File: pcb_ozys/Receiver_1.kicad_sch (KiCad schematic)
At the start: 16 parts, among them Q4 2N7002, Q6 AO3401A, U1 INA826AIDR

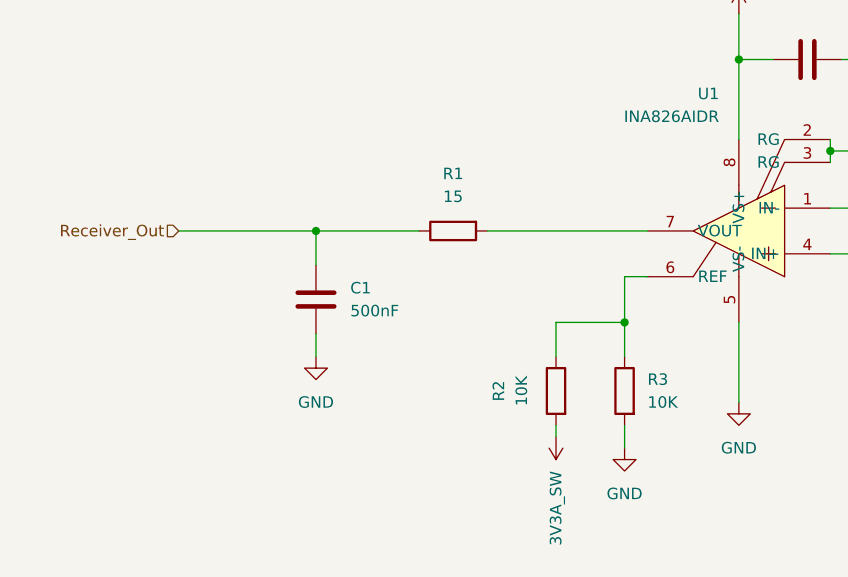
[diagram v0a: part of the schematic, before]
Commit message: Started PCBs fixed connectors
- Fixed Bypass on CAN
- Seperated SG connectors from 2x1 to 1x1
- Rough Draft of Epsilon
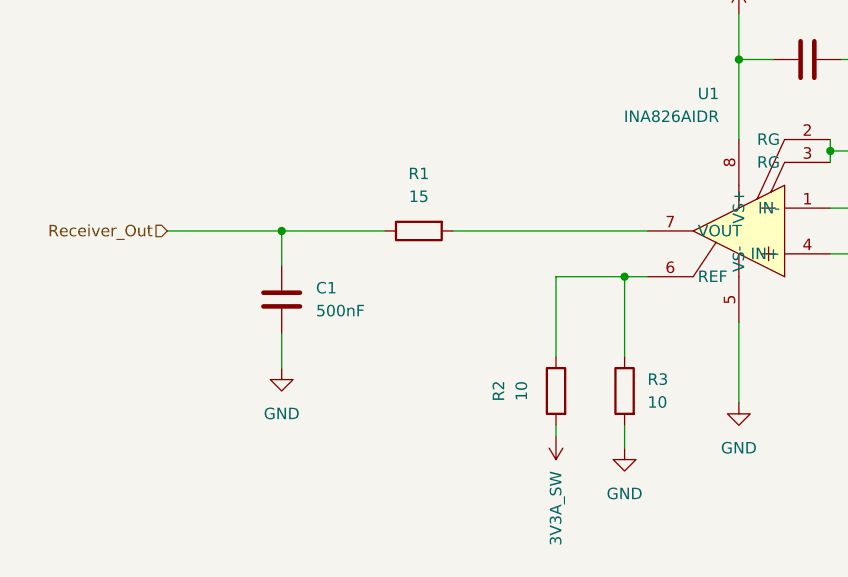
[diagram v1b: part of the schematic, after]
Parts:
- R2, R3: value 10K -> 10
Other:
- moved on the sheet: C1, R1
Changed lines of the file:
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@@
 	(paper "A4")
+	(junction
+		(at 129.54 130.81)
+		(diameter 0)
+		(color 0 0 0 0)
+	)
 	(junction
 		(at 100.33 71.12)
@@
 	)
 	(junction
-		(at 129.54 135.89)
-		(diameter 0)
-		(color 0 0 0 0)
-	)
-	(junction
 		(at 171.45 128.27)
 		(diameter 0)
@@
 	)
 	(junction
-		(at 95.25 125.73)
+		(at 91.44 125.73)
 		(diameter 0)
 		(color 0 0 0 0)
@@
 	(wire
 		(pts
-			(xy 80.01 125.73) (xy 95.25 125.73)
+			(xy 78.74 125.73) (xy 91.44 125.73)
 		)
 		(stroke
@@
 	(wire
 		(pts
-			(xy 95.25 125.73) (xy 106.68 125.73)
+			(xy 91.44 125.73) (xy 102.87 125.73)
 		)
 		(stroke
@@
 	(wire
 		(pts
-			(xy 95.25 129.54) (xy 95.25 125.73)
+			(xy 91.44 129.54) (xy 91.44 125.73)
 		)
 		(stroke
@@
 	(wire
 		(pts
-			(xy 121.92 135.89) (xy 121.92 139.7)
+			(xy 121.92 130.81) (xy 121.92 139.7)
 		)
 		(stroke
@@
 	(wire
 		(pts
-			(xy 129.54 135.89) (xy 129.54 130.81)
+			(xy 129.54 130.81) (xy 129.54 139.7)
 		)
 		(stroke
@@
 	(wire
 		(pts
-			(xy 95.25 137.16) (xy 95.25 139.7)
+			(xy 91.44 137.16) (xy 91.44 140.97)
 		)
 		(stroke
@@
 	(wire
 		(pts
-			(xy 121.92 135.89) (xy 129.54 135.89)
+			(xy 121.92 130.81) (xy 129.54 130.81)
 		)
 		(stroke
@@
 	(wire
 		(pts
-			(xy 132.08 125.73) (xy 114.3 125.73)
+			(xy 132.08 125.73) (xy 110.49 125.73)
 		)
 		(stroke
@@
 		(pts
 			(xy 193.04 97.79) (xy 208.28 97.79)
-		)
-		(stroke
-			(width 0)
-			(type default)
-		)
-	)
-	(wire
-		(pts
-			(xy 129.54 135.89) (xy 129.54 139.7)
 		)
 		(stroke
@@
 	(hierarchical_label "Receiver_Out"
 		(shape input)
-		(at 80.01 125.73 180)
+		(at 78.74 125.73 180)
 		(fields_autoplaced yes)
 		(effects
@@
 			)
 		)
-		(property "Value" "10K"
+		(property "Value" "10"
 			(at 132.08 144.7799 0)
 			(effects
@@
 	(symbol
 		(lib_id "Device:R")
-		(at 110.49 125.73 90)
+		(at 106.68 125.73 90)
 		(mirror x)
 		(unit 1)
@@
 		(fields_autoplaced yes)
 		(property "Reference" "R1"
-			(at 110.49 119.38 90)
+			(at 106.68 119.38 90)
 			(effects
 				(font
@@
 		)
 		(property "Value" "15"
-			(at 110.49 121.92 90)
+			(at 106.68 121.92 90)
 			(effects
 				(font
@@
 		)
 		(property "Footprint" ""
-			(at 110.49 123.952 90)
+			(at 106.68 123.952 90)
 			(effects
 				(font
@@
 		)
 		(property "Datasheet" "~"
-			(at 110.49 125.73 0)
+			(at 106.68 125.73 0)
 			(effects
 				(font
@@
 		)
 		(property "Description" "Resistor"
-			(at 110.49 125.73 0)
+			(at 106.68 125.73 0)
 			(effects
 				(font
@@
 	(symbol
 		(lib_id "power:GND")
-		(at 95.25 139.7 0)
+		(at 91.44 140.97 0)
 		(unit 1)
 		(exclude_from_sim no)
@@
 		(fields_autoplaced yes)
 		(property "Reference" "#PWR01"
-			(at 95.25 146.05 0)
+			(at 91.44 147.32 0)
 			(effects
 				(font
@@
 		)
 		(property "Value" "GND"
-			(at 95.25 144.78 0)
+			(at 91.44 146.05 0)
 			(effects
 				(font
@@
 		)
 		(property "Footprint" ""
-			(at 95.25 139.7 0)
+			(at 91.44 140.97 0)
 			(effects
 				(font
@@
 		)
 		(property "Datasheet" ""
-			(at 95.25 139.7 0)
+			(at 91.44 140.97 0)
 			(effects
 				(font
@@
 		)
 		(property "Description" "Power symbol creates a global label with name \"GND\" , ground"
-			(at 95.25 139.7 0)
+			(at 91.44 140.97 0)
 			(effects
 				(font
@@
 	(symbol
 		(lib_id "Device:C")
-		(at 95.25 133.35 0)
+		(at 91.44 133.35 0)
 		(unit 1)
 		(exclude_from_sim no)
@@
 		(fields_autoplaced yes)
 		(property "Reference" "C1"
-			(at 99.06 132.0799 0)
+			(at 95.25 132.0799 0)
 			(effects
 				(font
@@
 		)
 		(property "Value" "500nF"
-			(at 99.06 134.6199 0)
+			(at 95.25 134.6199 0)
 			(effects
 				(font
@@
 		)
 		(property "Footprint" ""
-			(at 96.2152 137.16 0)
+			(at 92.4052 137.16 0)
 			(effects
 				(font
@@
 		)
 		(property "Datasheet" "~"
-			(at 95.25 133.35 0)
+			(at 91.44 133.35 0)
 			(effects
 				(font
@@
 		)
 		(property "Description" "Unpolarized capacitor"
-			(at 95.25 133.35 0)
+			(at 91.44 133.35 0)
 			(effects
 				(font
@@
 			)
 		)
-		(property "Value" "10K"
+		(property "Value" "10"
 			(at 118.11 143.51 90)
 			(effects
